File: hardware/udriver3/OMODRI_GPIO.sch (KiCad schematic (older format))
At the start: 5 parts, among them U17 TPD2E001, U18 TPD2E001, U19 TPD2E001, U20 TPD2E001, U3 TMS320F28388D

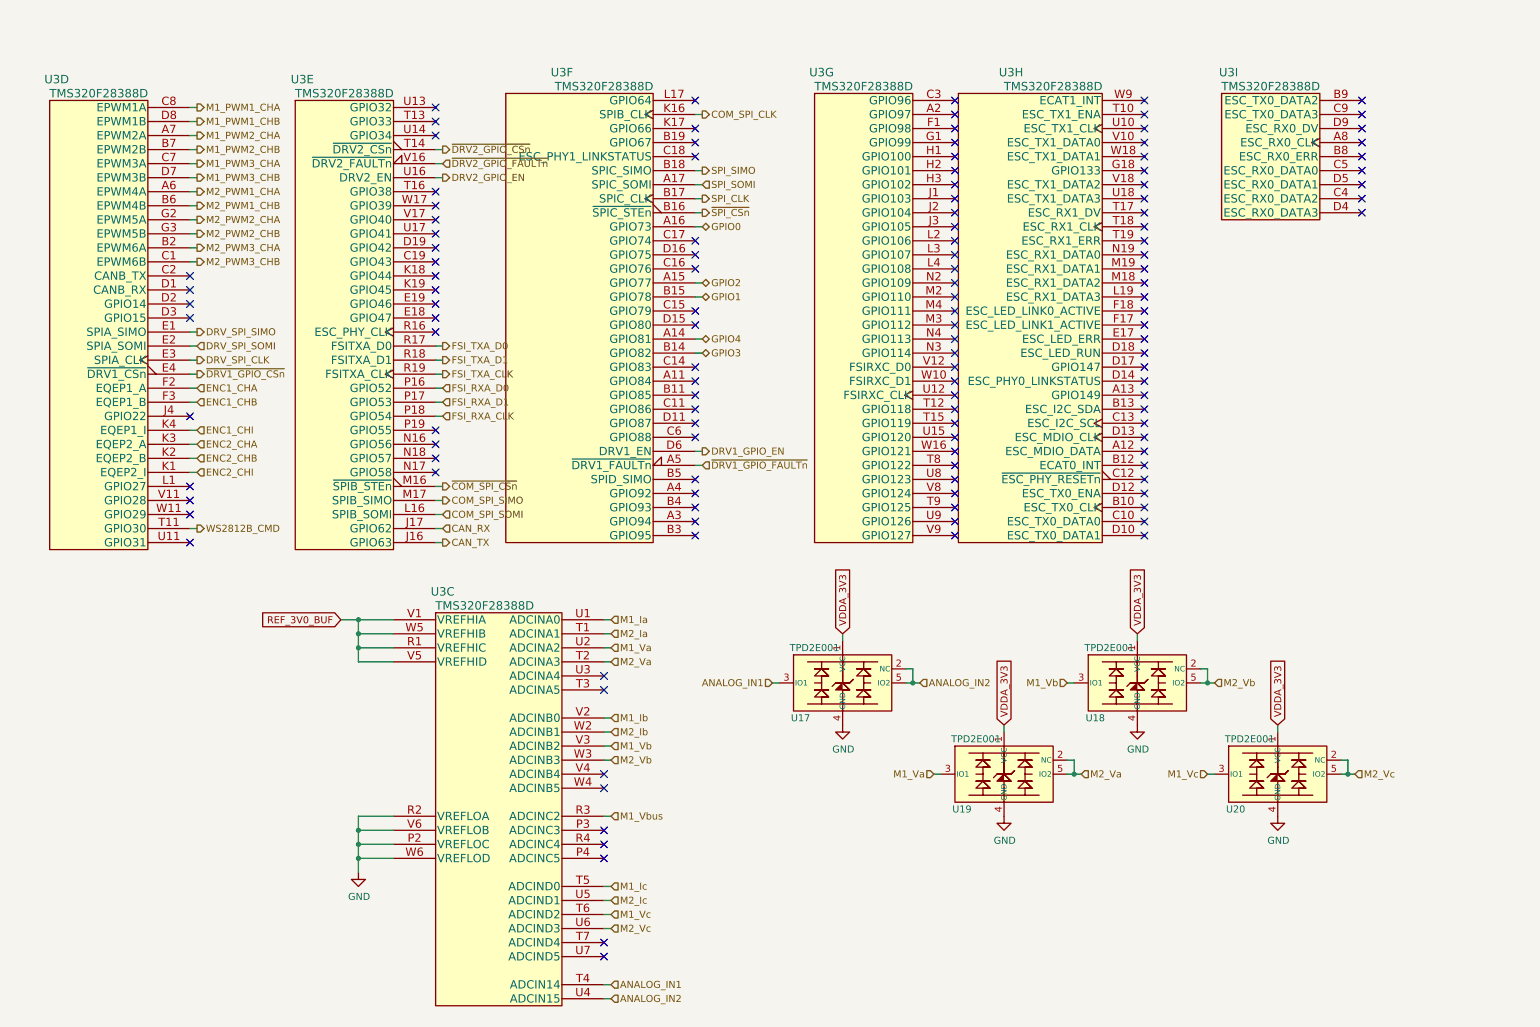
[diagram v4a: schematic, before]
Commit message: Update of the schematics. Driver and power files split. Placement starting.
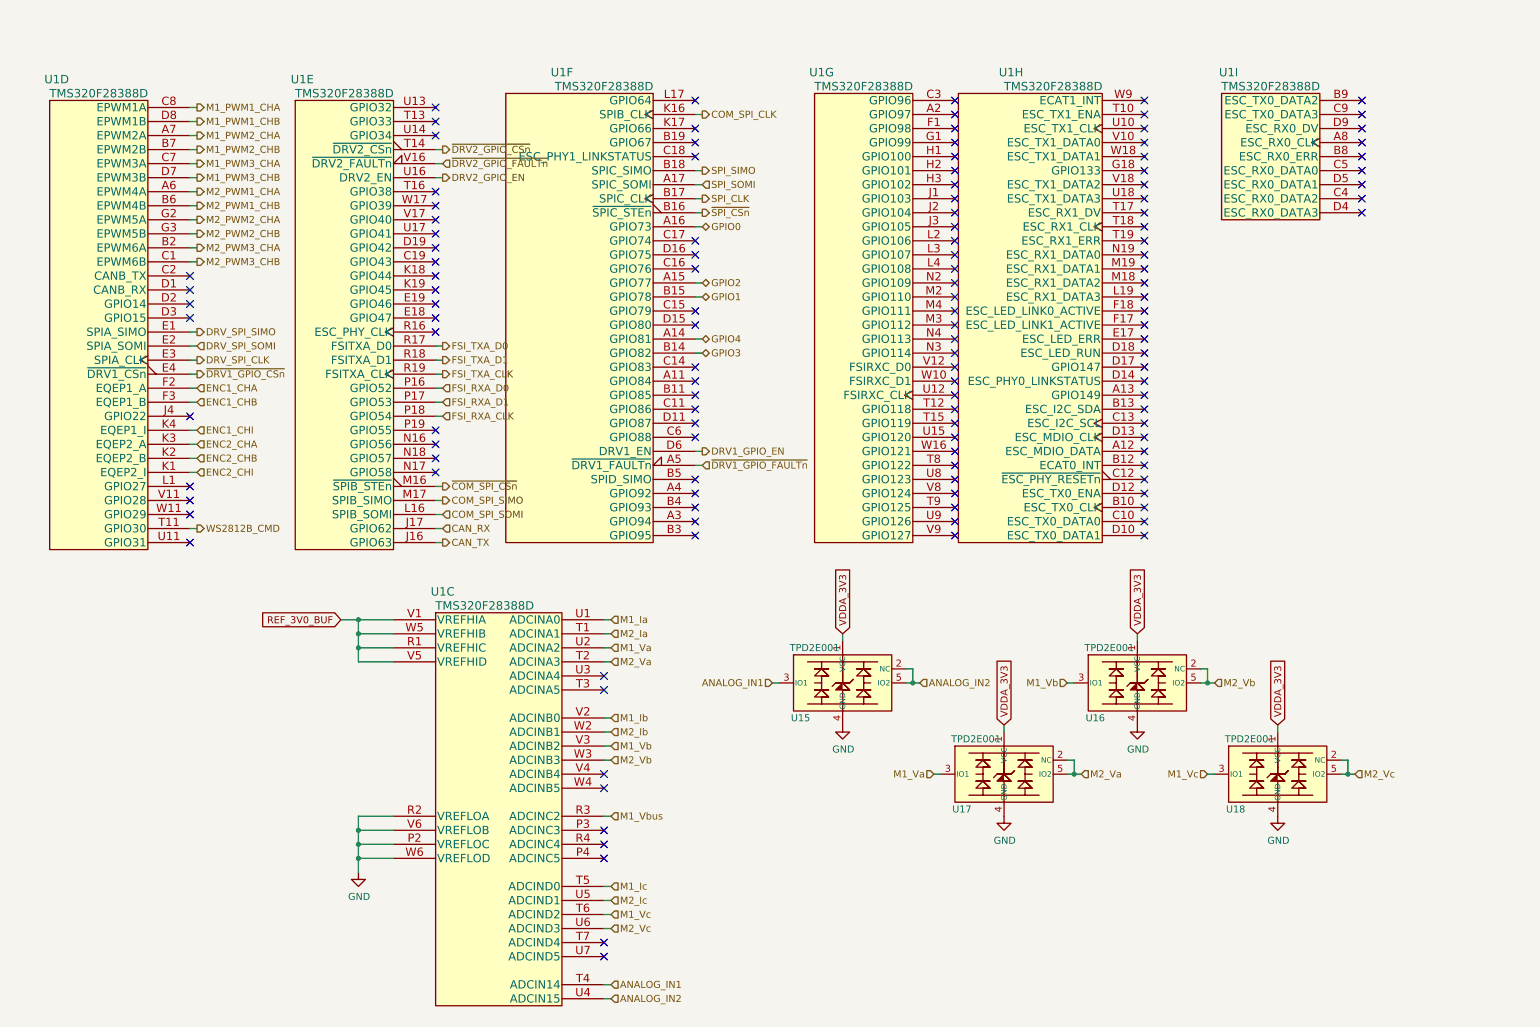
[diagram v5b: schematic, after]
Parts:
- U1: renamed from U3; footprint udrive3:NFBGA_337 -> udriver3:NFBGA_337
- renumbered U17 to U15, U18 to U16, U19 to U17, U20 to U18
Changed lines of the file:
@@
 $Descr A4 11693 8268
 encoding utf-8
-Sheet 10 10
+Sheet 13 17
 Title "Open MOtor DRiver Initiative (OMODRI)"
 Date ""
@@
 P 1050 3050
 AR Path="/5F3A5338/5F3A5B71" Ref="U?"  Part="4"
-AR Path="/5F5975A7/5F3A5B71" Ref="U3"  Part="4"
-F 0 "U3" H 750 5150 60  0000 C CNN
+AR Path="/5F5975A7/5F3A5B71" Ref="U1"  Part="4"
+F 0 "U1" H 750 5150 60  0000 C CNN
 F 1 "TMS320F28388D" H 1050 5050 60  0000 C CNN
-F 2 "udrive3:NFBGA_337" H 1050 5050 60  0001 C CNN
+F 2 "udriver3:NFBGA_337" H 1050 5050 60  0001 C CNN
 F 3 "https://www.ti.com/lit/ds/symlink/tms320f28388d.pdf" H 1208 5101 60  0001 C CNN
 F 4 " 	296-F28388DZWTS-ND" H 1050 3050 50  0001 C CNN "DigiKey"
@@
 P 2800 3050
 AR Path="/5F3A5338/5F3AD210" Ref="U?"  Part="5"
-AR Path="/5F5975A7/5F3AD210" Ref="U3"  Part="5"
-F 0 "U3" H 2500 5150 60  0000 C CNN
+AR Path="/5F5975A7/5F3AD210" Ref="U1"  Part="5"
+F 0 "U1" H 2500 5150 60  0000 C CNN
 F 1 "TMS320F28388D" H 2800 5050 60  0000 C CNN
-F 2 "udrive3:NFBGA_337" H 2800 5050 60  0001 C CNN
+F 2 "udriver3:NFBGA_337" H 2800 5050 60  0001 C CNN
 F 3 "https://www.ti.com/lit/ds/symlink/tms320f28388d.pdf" H 2958 5101 60  0001 C CNN
 F 4 " 	296-F28388DZWTS-ND" H 2800 3050 50  0001 C CNN "DigiKey"
@@
 P 4650 3000
 AR Path="/5F3A5338/5F3C0127" Ref="U?"  Part="6"
-AR Path="/5F5975A7/5F3C0127" Ref="U3"  Part="6"
-F 0 "U3" H 4350 5100 60  0000 C CNN
+AR Path="/5F5975A7/5F3C0127" Ref="U1"  Part="6"
+F 0 "U1" H 4350 5100 60  0000 C CNN
 F 1 "TMS320F28388D" H 4650 5000 60  0000 C CNN
-F 2 "udrive3:NFBGA_337" H 4650 5000 60  0001 C CNN
+F 2 "udriver3:NFBGA_337" H 4650 5000 60  0001 C CNN
 F 3 "https://www.ti.com/lit/ds/symlink/tms320f28388d.pdf" H 4808 5051 60  0001 C CNN
 F 4 " 	296-F28388DZWTS-ND" H 4650 3000 50  0001 C CNN "DigiKey"
@@
 P 6500 3000
 AR Path="/5F3A5338/5F3CEA6B" Ref="U?"  Part="7"
-AR Path="/5F5975A7/5F3CEA6B" Ref="U3"  Part="7"
-F 0 "U3" H 6200 5100 60  0000 C CNN
+AR Path="/5F5975A7/5F3CEA6B" Ref="U1"  Part="7"
+F 0 "U1" H 6200 5100 60  0000 C CNN
 F 1 "TMS320F28388D" H 6500 5000 60  0000 C CNN
-F 2 "udrive3:NFBGA_337" H 6500 5000 60  0001 C CNN
+F 2 "udriver3:NFBGA_337" H 6500 5000 60  0001 C CNN
 F 3 "https://www.ti.com/lit/ds/symlink/tms320f28388d.pdf" H 6658 5051 60  0001 C CNN
 F 4 " 	296-F28388DZWTS-ND" H 6500 3000 50  0001 C CNN "DigiKey"
@@
 P 7850 3000
 AR Path="/5F3A5338/5F3D4214" Ref="U?"  Part="8"
-AR Path="/5F5975A7/5F3D4214" Ref="U3"  Part="8"
-F 0 "U3" H 7550 5100 60  0000 C CNN
+AR Path="/5F5975A7/5F3D4214" Ref="U1"  Part="8"
+F 0 "U1" H 7550 5100 60  0000 C CNN
 F 1 "TMS320F28388D" H 7850 5000 60  0000 C CNN
-F 2 "udrive3:NFBGA_337" H 7850 5000 60  0001 C CNN
+F 2 "udriver3:NFBGA_337" H 7850 5000 60  0001 C CNN
 F 3 "https://www.ti.com/lit/ds/symlink/tms320f28388d.pdf" H 8008 5051 60  0001 C CNN
 F 4 " 	296-F28388DZWTS-ND" H 7850 3000 50  0001 C CNN "DigiKey"
@@
 P 3900 6700
 AR Path="/5F3A5338/5F3B32A9" Ref="U?"  Part="3"
-AR Path="/5F5975A7/5F3B32A9" Ref="U3"  Part="3"
-F 0 "U3" H 3500 8800 60  0000 C CNN
+AR Path="/5F5975A7/5F3B32A9" Ref="U1"  Part="3"
+F 0 "U1" H 3500 8800 60  0000 C CNN
 F 1 "TMS320F28388D" H 3800 8700 60  0000 C CNN
-F 2 "udrive3:NFBGA_337" H 3900 8700 60  0001 C CNN
+F 2 "udriver3:NFBGA_337" H 3900 8700 60  0001 C CNN
 F 3 "https://www.ti.com/lit/ds/symlink/tms320f28388d.pdf" H 3900 8751 60  0001 C CNN
 F 4 " 	296-F28388DZWTS-ND" H 3900 6700 50  0001 C CNN "DigiKey"
@@
 AR Path="/5F3A3F16/60145C31" Ref="#PWR?"  Part="1"
 AR Path="/5F3A5338/60145C31" Ref="#PWR?"  Part="1"
-AR Path="/5F5975A7/60145C31" Ref="#PWR0141"  Part="1"
-F 0 "#PWR0141" H 2900 6350 50  0001 C CNN
+AR Path="/5F5975A7/60145C31" Ref="#PWR098"  Part="1"
+F 0 "#PWR098" H 2900 6350 50  0001 C CNN
 F 1 "GND" H 2905 6427 50  0000 C CNN
 F 2 "" H 2900 6600 50  0001 C CNN
@@
 P 9400 3000
 AR Path="/5F3A5338/5F3DE432" Ref="U?"  Part="9"
-AR Path="/5F5975A7/5F3DE432" Ref="U3"  Part="9"
-F 0 "U3" H 9100 5100 60  0000 C CNN
+AR Path="/5F5975A7/5F3DE432" Ref="U1"  Part="9"
+F 0 "U1" H 9100 5100 60  0000 C CNN
 F 1 "TMS320F28388D" H 9400 5000 60  0000 C CNN
-F 2 "udrive3:NFBGA_337" H 9400 5000 60  0001 C CNN
+F 2 "udriver3:NFBGA_337" H 9400 5000 60  0001 C CNN
 F 3 "https://www.ti.com/lit/ds/symlink/tms320f28388d.pdf" H 9558 5051 60  0001 C CNN
 F 4 " 	296-F28388DZWTS-ND" H 9400 3000 50  0001 C CNN "DigiKey"
@@
 P 9450 5900
 AR Path="/5F3A5338/62D1CA86" Ref="U?"  Part="1"
-AR Path="/5F5975A7/62D1CA86" Ref="U20"  Part="1"
-F 0 "U20" H 9150 5650 50  0000 C CNN
+AR Path="/5F5975A7/62D1CA86" Ref="U18"  Part="1"
+F 0 "U18" H 9150 5650 50  0000 C CNN
 F 1 "TPD2E001" H 9250 6150 50  0000 C CNN
 F 2 "Package_SO:Texas_R-PDSO-N5" H 9400 5900 50  0001 C CNN
@@
 AR Path="/5F3A3F16/62D29CDB" Ref="#PWR?"  Part="1"
 AR Path="/5F3A5338/62D29CDB" Ref="#PWR?"  Part="1"
-AR Path="/5F5975A7/62D29CDB" Ref="#PWR0140"  Part="1"
-F 0 "#PWR0140" H 9450 5950 50  0001 C CNN
+AR Path="/5F5975A7/62D29CDB" Ref="#PWR097"  Part="1"
+F 0 "#PWR097" H 9450 5950 50  0001 C CNN
 F 1 "GND" H 9455 6027 50  0000 C CNN
 F 2 "" H 9450 6200 50  0001 C CNN
@@
 P 7500 5900
 AR Path="/5F3A5338/62D4FCEF" Ref="U?"  Part="1"
-AR Path="/5F5975A7/62D4FCEF" Ref="U19"  Part="1"
-F 0 "U19" H 7200 5650 50  0000 C CNN
+AR Path="/5F5975A7/62D4FCEF" Ref="U17"  Part="1"
+F 0 "U17" H 7200 5650 50  0000 C CNN
 F 1 "TPD2E001" H 7300 6150 50  0000 C CNN
 F 2 "Package_SO:Texas_R-PDSO-N5" H 7450 5900 50  0001 C CNN
@@
 AR Path="/5F3A3F16/62D4FCF7" Ref="#PWR?"  Part="1"
 AR Path="/5F3A5338/62D4FCF7" Ref="#PWR?"  Part="1"
-AR Path="/5F5975A7/62D4FCF7" Ref="#PWR0139"  Part="1"
-F 0 "#PWR0139" H 7500 5950 50  0001 C CNN
+AR Path="/5F5975A7/62D4FCF7" Ref="#PWR096"  Part="1"
+F 0 "#PWR096" H 7500 5950 50  0001 C CNN
 F 1 "GND" H 7505 6027 50  0000 C CNN
 F 2 "" H 7500 6200 50  0001 C CNN
@@
 P 8450 5250
 AR Path="/5F3A5338/62D6E35F" Ref="U?"  Part="1"
-AR Path="/5F5975A7/62D6E35F" Ref="U18"  Part="1"
-F 0 "U18" H 8150 5000 50  0000 C CNN
+AR Path="/5F5975A7/62D6E35F" Ref="U16"  Part="1"
+F 0 "U16" H 8150 5000 50  0000 C CNN
 F 1 "TPD2E001" H 8250 5500 50  0000 C CNN
 F 2 "Package_SO:Texas_R-PDSO-N5" H 8400 5250 50  0001 C CNN
@@
 AR Path="/5F3A3F16/62D6E367" Ref="#PWR?"  Part="1"
 AR Path="/5F3A5338/62D6E367" Ref="#PWR?"  Part="1"
-AR Path="/5F5975A7/62D6E367" Ref="#PWR0138"  Part="1"
-F 0 "#PWR0138" H 8450 5300 50  0001 C CNN
+AR Path="/5F5975A7/62D6E367" Ref="#PWR095"  Part="1"
+F 0 "#PWR095" H 8450 5300 50  0001 C CNN
 F 1 "GND" H 8455 5377 50  0000 C CNN
 F 2 "" H 8450 5550 50  0001 C CNN
@@
 P 6350 5250
 AR Path="/5F3A5338/62D88EDA" Ref="U?"  Part="1"
-AR Path="/5F5975A7/62D88EDA" Ref="U17"  Part="1"
-F 0 "U17" H 6050 5000 50  0000 C CNN
+AR Path="/5F5975A7/62D88EDA" Ref="U15"  Part="1"
+F 0 "U15" H 6050 5000 50  0000 C CNN
 F 1 "TPD2E001" H 6150 5500 50  0000 C CNN
 F 2 "Package_SO:Texas_R-PDSO-N5" H 6300 5250 50  0001 C CNN
@@
 AR Path="/5F3A3F16/62D88EE2" Ref="#PWR?"  Part="1"
 AR Path="/5F3A5338/62D88EE2" Ref="#PWR?"  Part="1"
-AR Path="/5F5975A7/62D88EE2" Ref="#PWR0137"  Part="1"
-F 0 "#PWR0137" H 6350 5300 50  0001 C CNN
+AR Path="/5F5975A7/62D88EE2" Ref="#PWR094"  Part="1"
+F 0 "#PWR094" H 6350 5300 50  0001 C CNN
 F 1 "GND" H 6355 5377 50  0000 C CNN
 F 2 "" H 6350 5550 50  0001 C CNN

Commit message: Update of the schematics. Switches on GPIO72 & GPIO84 are missing. J1, J2 & J14 must be merged and connector placement optimized. TCXO must be changed from 20MHz to 25MHz for EtherCAT compatibility. PCB is partially routed in 6-Layers (mainly power supplies and and transistors). 8-Layers will be necessary.
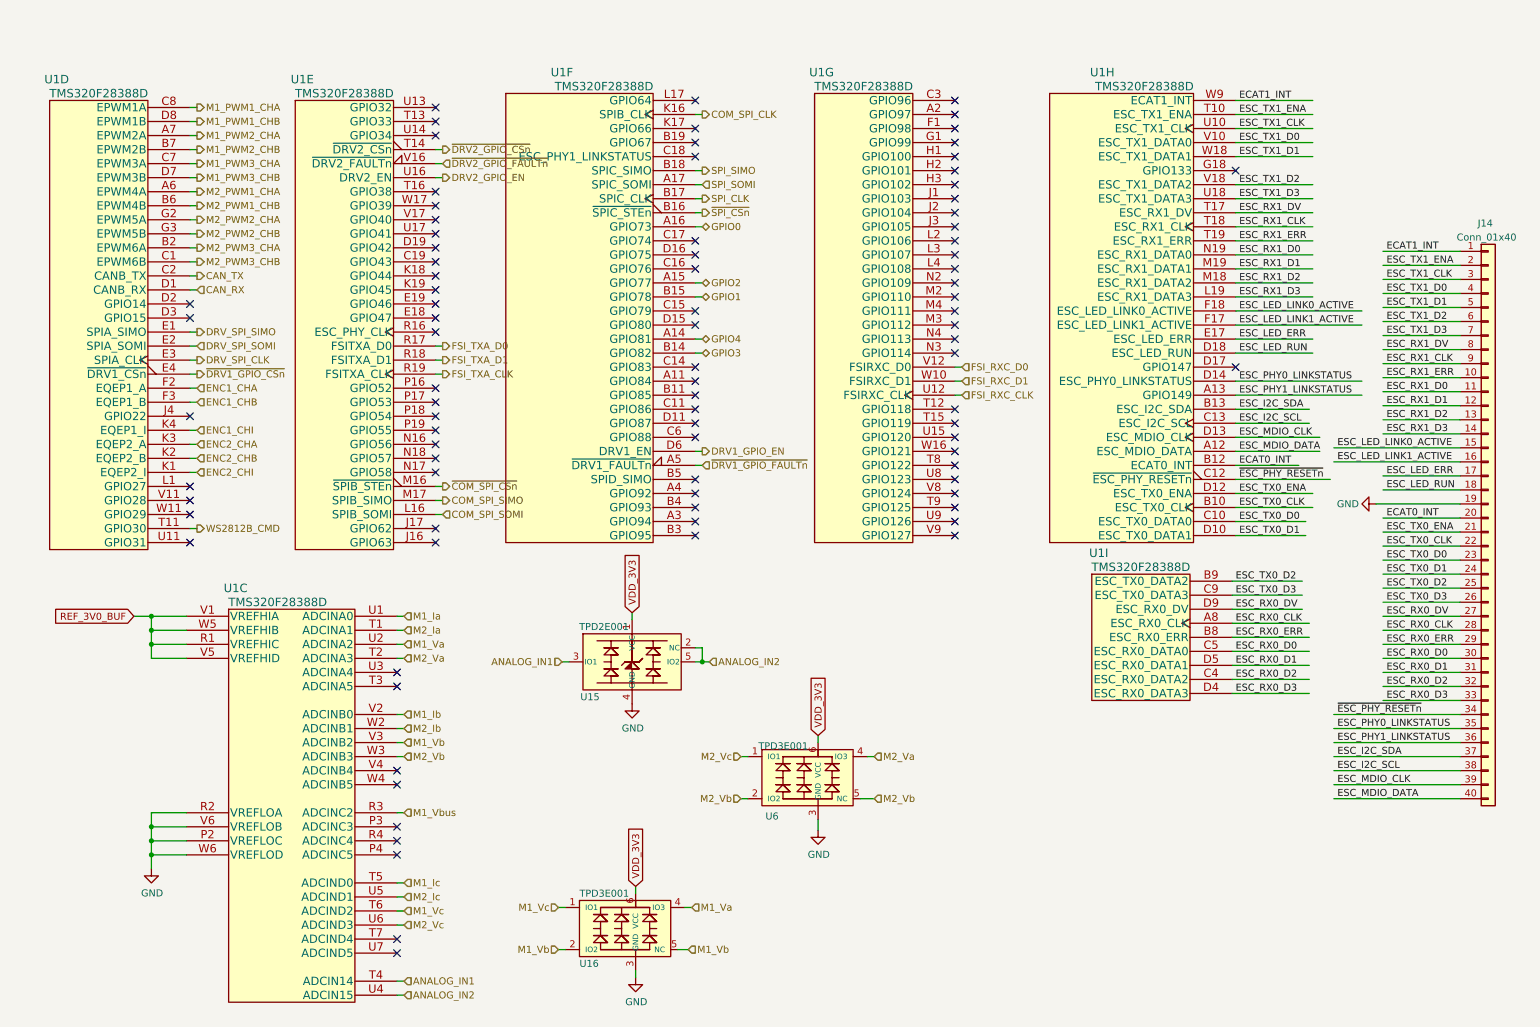
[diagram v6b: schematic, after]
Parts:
- removed U16, U17, U18: TPD2E001, Package_SO:Texas_R-PDSO-N5, symbol omodri_lib:TPD2E001
- added J14: Conn_01x40, Connector_FFC-FPC:JAE_FF0841SA1_2Rows-41Pins_P0.40mm_Horizontal, symbol Connector_Generic:Conn_01x40
- added U16, U6: TPD3E001, udriver3:USON_6, symbol omodri_lib:TPD3E001
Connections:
- net labels added: ECAT0_INT, ECAT1_INT, ESC_I2C_SCL, ESC_I2C_SDA, ESC_LED_ERR, ESC_LED_LINK0_ACTIVE, ESC_LED_LINK1_ACTIVE, ESC_LED_RUN, ESC_MDIO_CLK, ESC_MDIO_DATA, ESC_PHY0_LINKSTATUS, ESC_PHY1_LINKSTATUS, ESC_RX0_CLK, ESC_RX0_D0, ESC_RX0_D1, ESC_RX0_D2, ESC_RX0_D3, ESC_RX0_DV, ESC_RX0_ERR, ESC_RX1_CLK, ESC_RX1_D0, ESC_RX1_D1, ESC_RX1_D2, ESC_RX1_D3, ESC_RX1_DV, ESC_RX1_ERR, ESC_TX0_CLK, ESC_TX0_D0, ESC_TX0_D1, ESC_TX0_D2, ESC_TX0_D3, ESC_TX0_ENA, ESC_TX1_CLK, ESC_TX1_D0, ESC_TX1_D1, ESC_TX1_D2, ESC_TX1_D3, ESC_TX1_ENA, FSI_RXC_CLK, FSI_RXC_D0, FSI_RXC_D1, VDD_3V3, ~ESC_PHY_RESETn~
- net labels removed: FSI_RXA_CLK, FSI_RXA_D0, FSI_RXA_D1, VDDA_3V3
- wire segments 104 -> 177
- no-connect marks 129 -> 90
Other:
- moved on the sheet: U15, U1C, U1H, U1I
